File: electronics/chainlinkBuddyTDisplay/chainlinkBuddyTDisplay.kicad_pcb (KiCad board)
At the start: 2 copper layers, 74.9 x 49.5 mm, 13 parts, among them J1 Output, J2 Screw_Terminal_01x03, J3 Barrel_Jack_Switch, J7 Conn_01x04, U1 TTGO_TDisplay, U2 LM7805_TO220

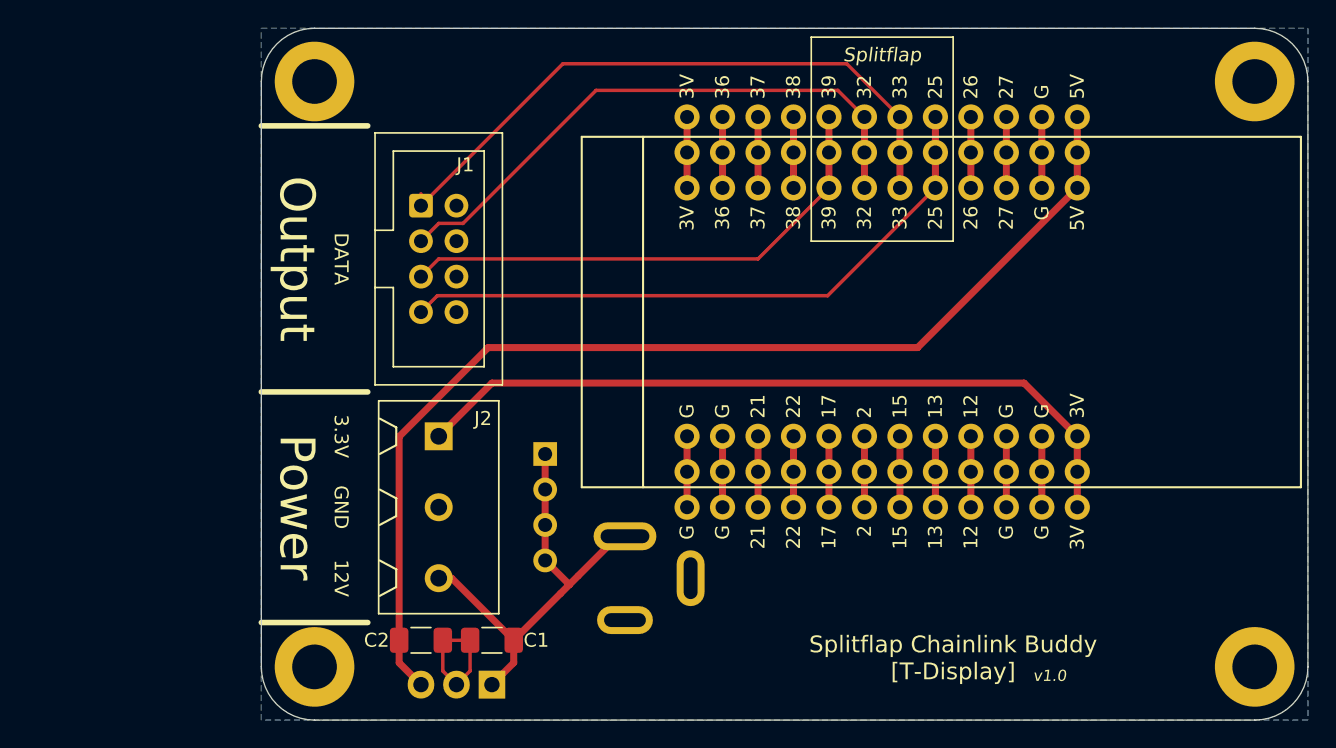
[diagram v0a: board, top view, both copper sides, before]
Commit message: More tweaks to Chainlink Driver, update Chainlink Buddy
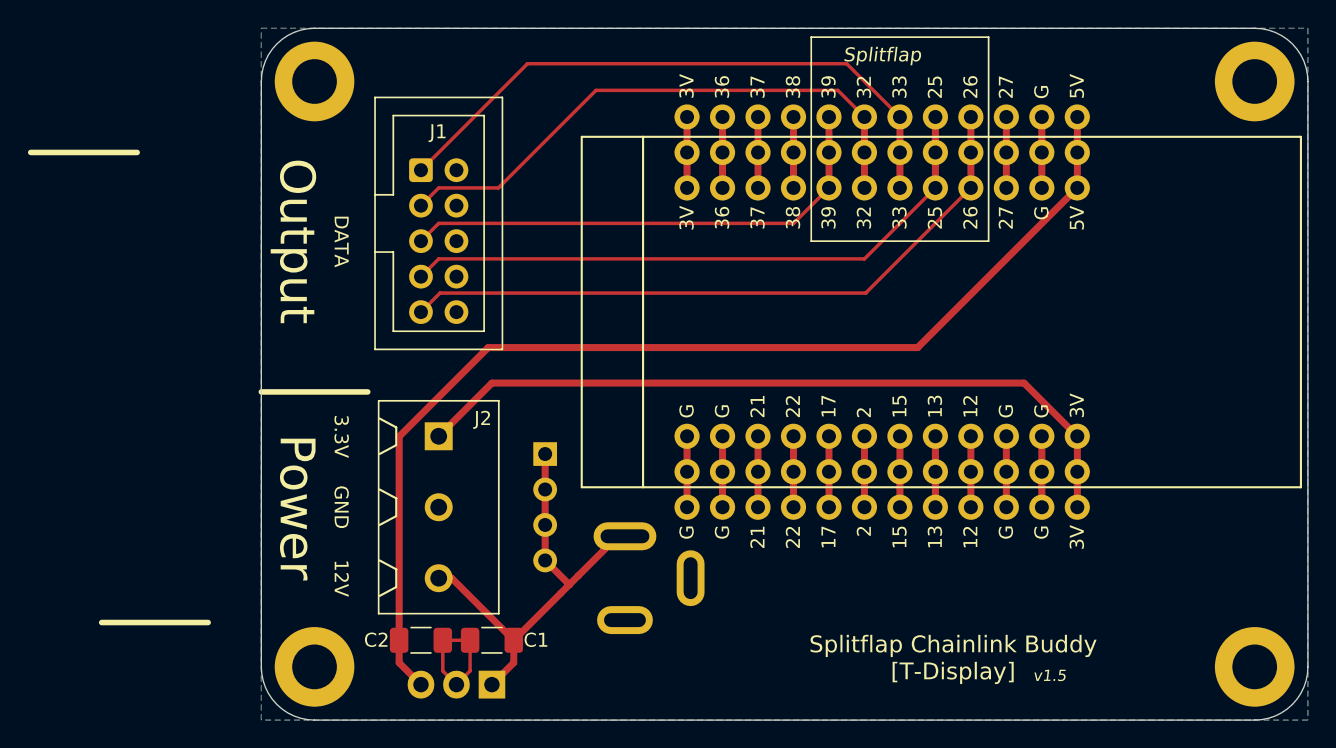
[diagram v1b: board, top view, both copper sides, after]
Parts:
- J1: footprint ModifiedSymbols:IDC-Header_2x04_P2.54mm_Vertical -> ModifiedSymbols:IDC-Header_2x05_P2.54mm_Vertical_2x04Silk
- moved J1 2.54 mm to (74.9, 73.7)
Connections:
- U1 pad 16: Net-(U1-Pad16) -> /nOE
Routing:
- net /nOE: track 0.00 -> 48.1 mm
- net Net-(U1-Pad16): track 5.08 -> 0.00 mm
- net /CLOCK: track 46.0 -> 44.1 mm
- net /SENSOR_DATA: track 36.9 -> 35.9 mm
- net /MOTOR_DATA: track 42.1 -> 41.0 mm
- net /LATCH: track 45.6 -> 44.5 mm
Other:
- board text added: "v1.5"
- board text added: "~Output en"
- board text removed: "v1.0"
